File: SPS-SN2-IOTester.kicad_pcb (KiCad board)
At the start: 2 copper layers, 33.2 x 55.5 mm, 26 parts, among them J1 RJ45, J2 Spade Terminal, SW1 SW, SW2 SW, SW3 SW, SW4 SW, SW5 SW, SW6 SW, SW7 SW, SW8 SW

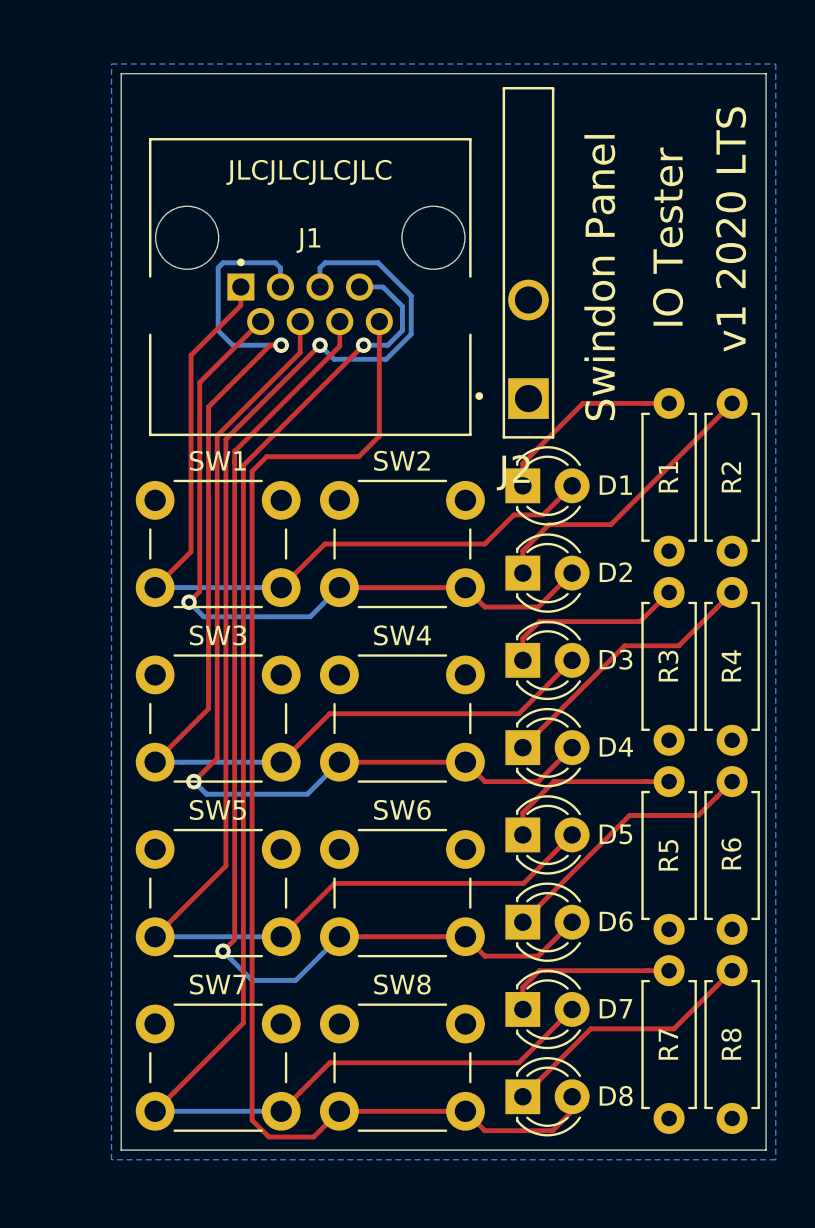
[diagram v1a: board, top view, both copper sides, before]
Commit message: added DC barrel jack and moved resistors
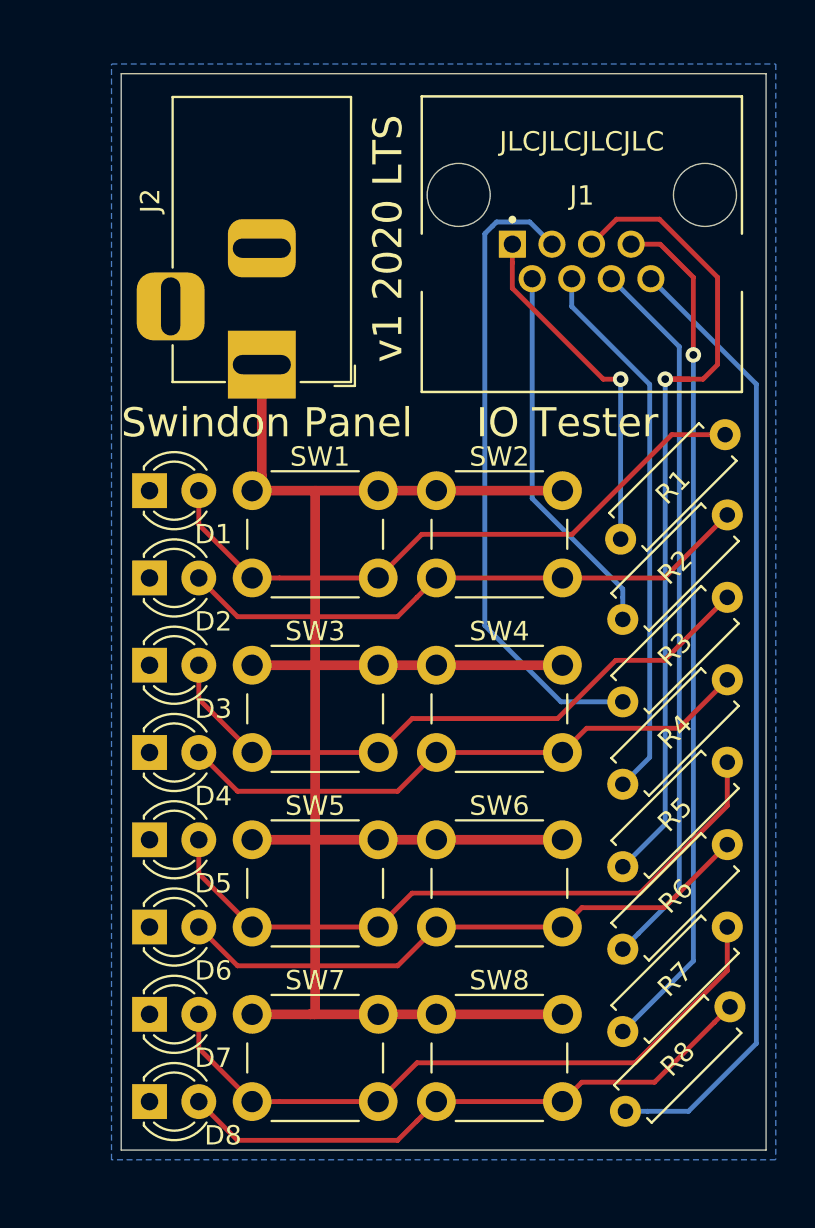
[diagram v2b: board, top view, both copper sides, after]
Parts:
- J2: value Spade Terminal -> Barrel_Jack; footprint libs:TE_928814-1 -> SamacSys_Parts:BarrelJack_Horizontal
- moved D1 19.3 mm to (86.0, 53.8)
- moved D2 19.3 mm to (86.0, 58.2)
- moved D3 19.3 mm to (86.0, 62.8)
- moved D4 19.3 mm to (86.0, 67.2)
- moved D5 19.3 mm to (86.0, 71.8)
- moved D6 19.3 mm to (86.0, 76.2)
- moved D7 19.3 mm to (86.0, 80.8)
- moved D8 19.3 mm to (86.0, 85.2)
- moved J1 14.2 mm to (108.2, 38.5)
- moved J2 13.9 mm to (91.8, 47.2), turned to 270 degrees
- moved R2 6.65 mm to (110.4, 60.4), turned to 45 degrees
- moved R4 6.08 mm to (110.4, 68.9), turned to 45 degrees
- moved R6 5.73 mm to (110.4, 77.4), turned to 45 degrees
- moved R8 5.51 mm to (110.5, 85.8), turned to 45 degrees
- moved R7 5.08 mm to (110.4, 81.6), turned to 45 degrees
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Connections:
- D1 pad 1: Net-(D1-Pad1) -> /GND
- D1 pad 2: /LINE1 -> Net-(D1-Pad2)
- D2 pad 1: Net-(D2-Pad1) -> /GND
- D2 pad 2: /LINE2 -> Net-(D2-Pad2)
- D3 pad 1: Net-(D3-Pad1) -> /GND
- D3 pad 2: /LINE3 -> Net-(D3-Pad2)
- D4 pad 1: Net-(D4-Pad1) -> /GND
- D4 pad 2: /LINE4 -> Net-(D4-Pad2)
- D5 pad 1: Net-(D5-Pad1) -> /GND
- D5 pad 2: /LINE5 -> Net-(D5-Pad2)
- D6 pad 1: Net-(D6-Pad1) -> /GND
- D6 pad 2: /LINE6 -> Net-(D6-Pad2)
- D7 pad 1: Net-(D7-Pad1) -> /GND
- D7 pad 2: /LINE7 -> Net-(D7-Pad2)
- D8 pad 1: Net-(D8-Pad1) -> /GND
- D8 pad 2: /LINE8 -> Net-(D8-Pad2)
- J2 pad 1: /COMMON -> /+24V
- J2 pad 2: (no net) -> /GND
- R1 pad 1: /COMMON -> /LINE1
- R1 pad 2: Net-(D1-Pad1) -> Net-(D1-Pad2)
- R2 pad 1: /COMMON -> /LINE2
- R2 pad 2: Net-(D2-Pad1) -> Net-(D2-Pad2)
- R3 pad 1: /COMMON -> /LINE3
- R3 pad 2: Net-(D3-Pad1) -> Net-(D3-Pad2)
- R4 pad 1: /COMMON -> /LINE4
- R4 pad 2: Net-(D4-Pad1) -> Net-(D4-Pad2)
- R5 pad 1: /COMMON -> /LINE5
- R5 pad 2: Net-(D5-Pad1) -> Net-(D5-Pad2)
- R6 pad 1: /COMMON -> /LINE6
- R6 pad 2: Net-(D6-Pad1) -> Net-(D6-Pad2)
- R7 pad 1: /COMMON -> /LINE7
- R7 pad 2: Net-(D7-Pad1) -> Net-(D7-Pad2)
- R8 pad 1: /COMMON -> /LINE8
- R8 pad 2: Net-(D8-Pad1) -> Net-(D8-Pad2)
- SW1 pad 1: /COMMON -> /+24V
- SW1 pad 2: /LINE1 -> Net-(D1-Pad2)
- SW2 pad 1: /COMMON -> /+24V
- SW2 pad 2: /LINE2 -> Net-(D2-Pad2)
- SW3 pad 1: /COMMON -> /+24V
- SW3 pad 2: /LINE3 -> Net-(D3-Pad2)
- SW4 pad 1: /COMMON -> /+24V
- SW4 pad 2: /LINE4 -> Net-(D4-Pad2)
- SW5 pad 1: /COMMON -> /+24V
- SW5 pad 2: /LINE5 -> Net-(D5-Pad2)
- SW6 pad 1: /COMMON -> /+24V
- SW6 pad 2: /LINE6 -> Net-(D6-Pad2)
- SW7 pad 1: /COMMON -> /+24V
- SW7 pad 2: /LINE7 -> Net-(D7-Pad2)
- SW8 pad 1: /COMMON -> /+24V
- SW8 pad 2: /LINE8 -> Net-(D8-Pad2)
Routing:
- net /+24V: track 0.00 -> 98.7 mm
- net Net-(D7-Pad2): track 0.00 -> 35.2 mm
- net Net-(D5-Pad2): track 0.00 -> 35.0 mm
- net Net-(D3-Pad2): track 0.00 -> 33.5 mm
- net Net-(D1-Pad2): track 0.00 -> 33.1 mm
- net Net-(D8-Pad2): track 0.00 -> 31.1 mm
- net Net-(D6-Pad2): track 0.00 -> 30.7 mm
- net Net-(D4-Pad2): track 0.00 -> 30.5 mm
- net Net-(D2-Pad2): track 0.00 -> 30.3 mm
- net /LINE7: track 73.8 -> 44.3 mm
- net /LINE5: track 71.7 -> 44.0 mm
- net /LINE3: track 59.4 -> 33.1 mm, vias 1 -> 0
- net /LINE1: track 41.2 -> 18.0 mm, vias 0 -> 1
- net /LINE4: track 47.5 -> 28.3 mm, vias 1 -> 0
- net /LINE6: track 55.7 -> 37.2 mm, vias 1 -> 0
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- added copper zone on B.Cu, net /GND
- removed copper zone on B.Cu, net /COMMON
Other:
- net class Fat added: clearance 0.2, trace_width 0.5, via_dia 0.8, via_drill 0.4

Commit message: swapped buttons and LEDs for enclosure versions
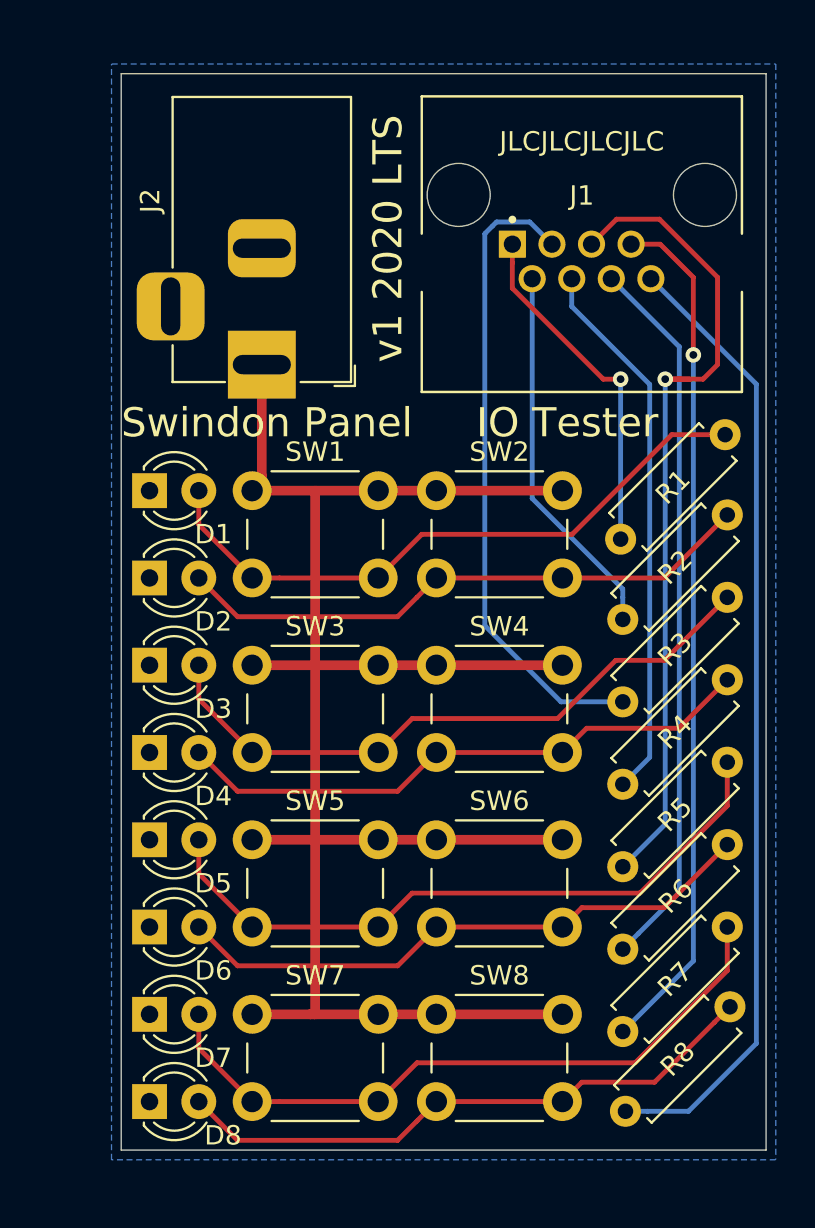
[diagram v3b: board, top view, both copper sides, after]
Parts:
- J2: footprint SamacSys_Parts:BarrelJack_Horizontal -> Connector_BarrelJack:BarrelJack_Horizontal
- SW1, SW2, SW3, SW4, SW5, SW6, SW7, SW8: footprint Button_Switch_THT:SW_PUSH_6mm_H5mm -> libs:SW_PUSH_6mm_H17mm

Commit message: Latest version with mounting holes
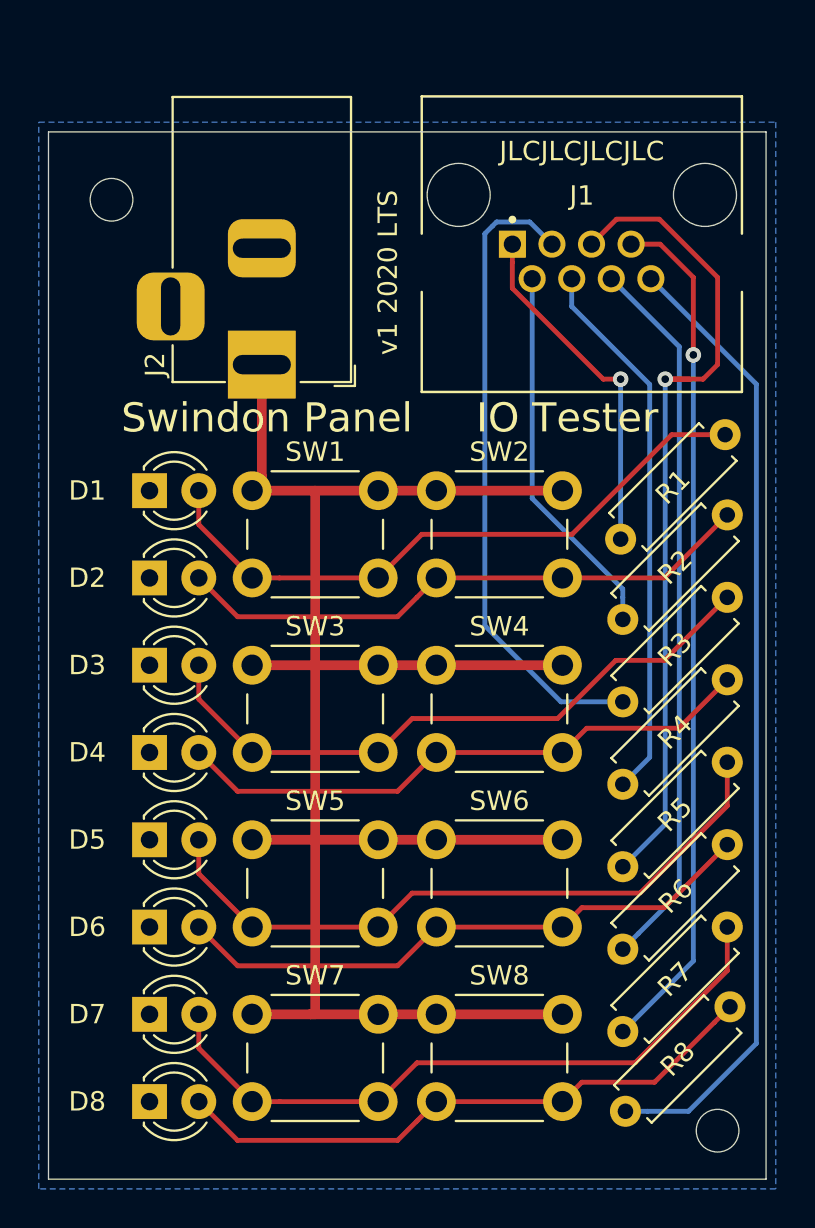
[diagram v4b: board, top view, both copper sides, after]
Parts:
- added H1: MountingHole, MountingHole:MountingHole_2.2mm_M2, F.Cu at (84.0, 38.8)
- added H2: MountingHole, MountingHole:MountingHole_2.2mm_M2, F.Cu at (115.2, 86.8)
- D1, D2, D3, D4, D5, D6, D7, D8: footprint LED_THT:LED_D3.0mm -> libs:LED_D3.0mm
- J2: footprint Connector_BarrelJack:BarrelJack_Horizontal -> SamacSys_Parts:BarrelJack_Horizontal
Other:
- board size 33.2 x 55.5 mm -> 37 x 54 mm

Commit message: Redesigned circuit to prevent switches blowing LEDs
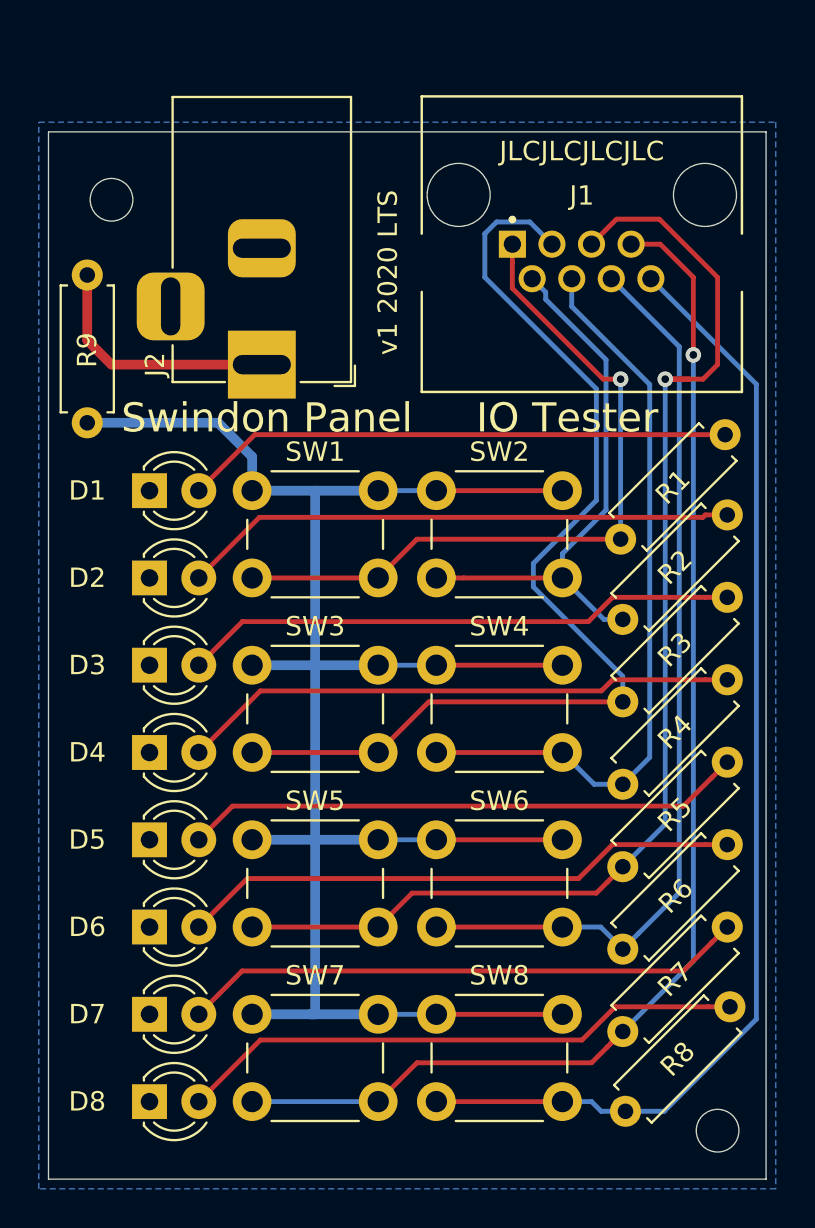
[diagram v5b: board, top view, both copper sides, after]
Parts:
- added R9: R, Resistor_THT:R_Axial_DIN0207_L6.3mm_D2.5mm_P7.62mm_Horizontal, F.Cu at (82.8, 50.2)
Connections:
- SW1 pad 1: /+24V -> Net-(R9-Pad1)
- SW1 pad 2: Net-(D1-Pad2) -> /LINE1
- SW2 pad 1: /+24V -> Net-(R9-Pad1)
- SW2 pad 2: Net-(D2-Pad2) -> /LINE2
- SW3 pad 1: /+24V -> Net-(R9-Pad1)
- SW3 pad 2: Net-(D3-Pad2) -> /LINE3
- SW4 pad 1: /+24V -> Net-(R9-Pad1)
- SW4 pad 2: Net-(D4-Pad2) -> /LINE4
- SW5 pad 1: /+24V -> Net-(R9-Pad1)
- SW5 pad 2: Net-(D5-Pad2) -> /LINE5
- SW6 pad 1: /+24V -> Net-(R9-Pad1)
- SW6 pad 2: Net-(D6-Pad2) -> /LINE6
- SW7 pad 1: /+24V -> Net-(R9-Pad1)
- SW7 pad 2: Net-(D7-Pad2) -> /LINE7
- SW8 pad 1: /+24V -> Net-(R9-Pad1)
- SW8 pad 2: Net-(D8-Pad2) -> /LINE8
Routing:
- net Net-(R9-Pad1): track 0.00 -> 102.5 mm
- net /+24V: track 98.7 -> 12.9 mm
- net /LINE7: track 44.3 -> 65.8 mm
- net /LINE3: track 33.1 -> 54.2 mm
- net /LINE5: track 44.0 -> 64.4 mm
- net /LINE1: track 18.0 -> 37.9 mm
- net /LINE4: track 28.3 -> 38.6 mm
- net /LINE6: track 37.2 -> 47.3 mm
- net /LINE8: track 49.9 -> 59.8 mm
- net /LINE2: track 19.5 -> 28.4 mm
- net Net-(D5-Pad2): track 35.0 -> 28.9 mm
- net Net-(D7-Pad2): track 35.2 -> 29.1 mm
- net Net-(D1-Pad2): track 33.1 -> 28.3 mm
- net Net-(D3-Pad2): track 33.5 -> 28.7 mm
- net Net-(D6-Pad2): track 30.7 -> 29.0 mm
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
